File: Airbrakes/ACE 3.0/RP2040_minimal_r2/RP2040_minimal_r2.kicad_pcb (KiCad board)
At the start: 2 copper layers, 52 x 51 mm, 44 parts, among them J1 USB_B_Micro, J2 Conn_01x02, J3 104031-0811, J4 Conn_02x18_Odd_Even, U1 NCP1117-3.3_SOT223, U2 W25Q128JVS, U3 RP2040, U4 BMI088, U5 BMP581, U6 BMM350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

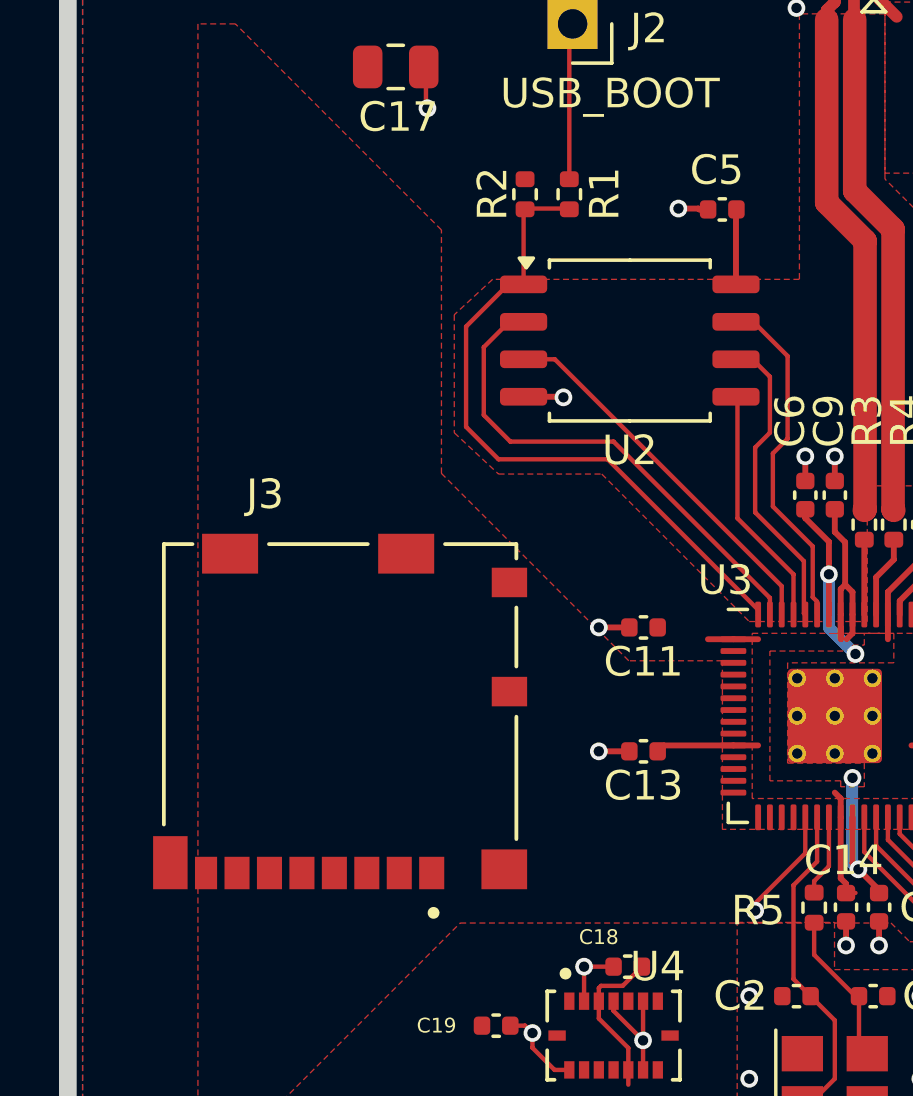
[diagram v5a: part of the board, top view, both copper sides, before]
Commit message: sd card interfacing
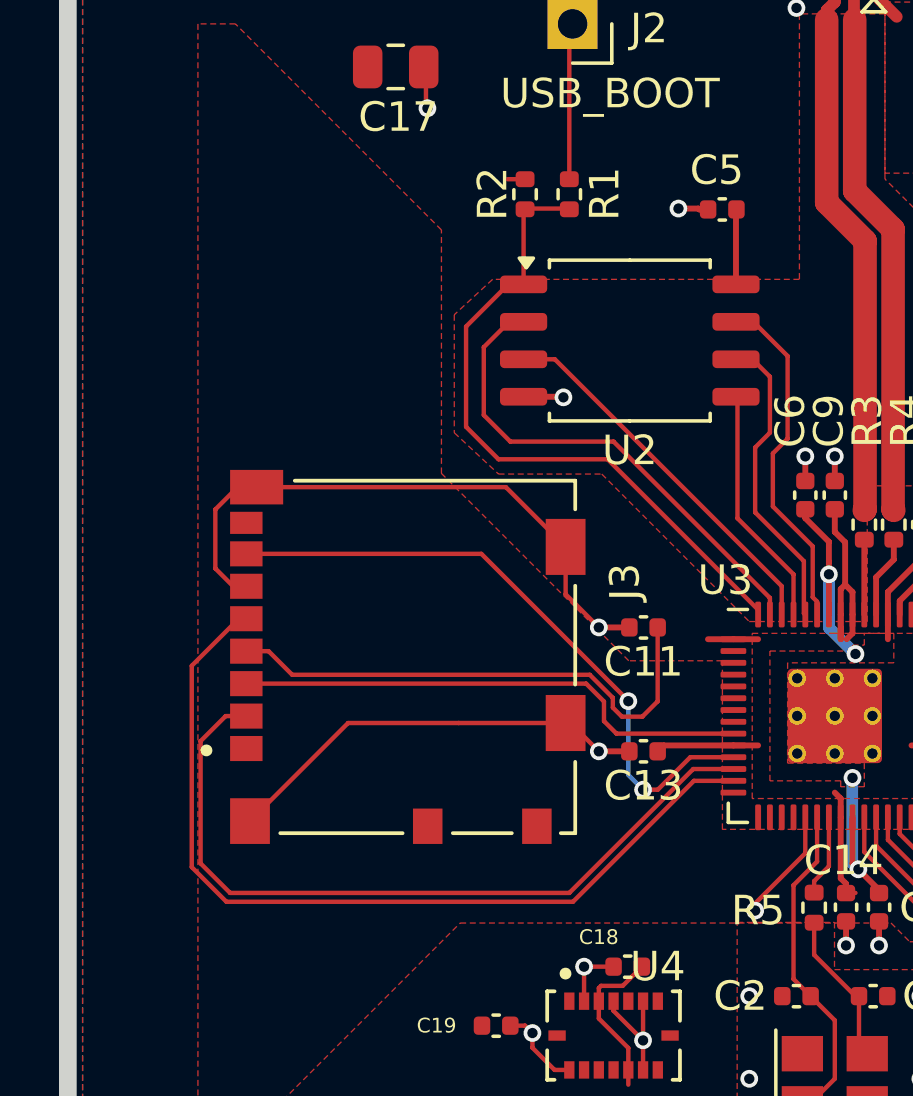
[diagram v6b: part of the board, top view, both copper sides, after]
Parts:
- moved J3 2.94 mm to (85.5, 98.0), turned to -90 degrees
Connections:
- J3 pad 2: unconnected-(J3-CD/DAT3-Pad2) -> /CS_SD
- J3 pad 3: unconnected-(J3-CMD-Pad3) -> /MOSI
- J3 pad 4: unconnected-(J3-VDD-Pad4) -> +3V3
- J3 pad 5: unconnected-(J3-CLK-Pad5) -> /SCLK
- J3 pad 6: unconnected-(J3-VSS-Pad6) -> GND
- J3 pad 7: unconnected-(J3-DAT0-Pad7) -> /MISO
- J3 pad G1: unconnected-(J3-GND-PadG1) -> GND
- J3 pad G2: unconnected-(J3-GND__1-PadG2) -> GND
- J3 pad G3: unconnected-(J3-GND__2-PadG3) -> GND
- J3 pad G4: unconnected-(J3-GND__3-PadG4) -> GND
- U3 pad 11: /GPIO8 -> /MISO
- U3 pad 12: /GPIO9 -> /CS_SD
- U3 pad 13: /GPIO10 -> /SCLK
- U3 pad 9: /GPIO7 -> /MOSI
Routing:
- net GND: track 46.5 -> 79.7 mm
- net /SCLK: track 0.00 -> 29.9 mm
- net /CS_SD: track 0.00 -> 26.3 mm
- net /MISO: track 0.00 -> 21.8 mm, vias 0 -> 2
- net +3V3: track 42.7 -> 61.3 mm
- net /MOSI: track 0.00 -> 17.6 mm
